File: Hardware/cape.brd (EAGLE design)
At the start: 123 x 126 mm, 38 parts, among them IC2 74VHC541, IC4 74VHC541, IC5 74VHC541, J3 RJ45-8P8C, Q1 N-MOSFET-DUALSO8, Q10 N-MOSFET-DUALSO8, Q11 N-MOSFET-DUALSO8, Q12 N-MOSFET-DUALSO8, Q13 N-MOSFET-DUALSO8, Q14 N-MOSFET-DUALSO8, Q15 N-MOSFET-DUALSO8, Q16 N-MOSFET-DUALSO8, Q2 N-MOSFET-DUALSO8, Q3 N-MOSFET-DUALSO8, Q4 N-MOSFET-DUALSO8, Q5 N-MOSFET-DUALSO8, Q6 N-MOSFET-DUALSO8, Q7 N-MOSFET-DUALSO8, Q8 N-MOSFET-DUALSO8, Q9 N-MOSFET-DUALSO8

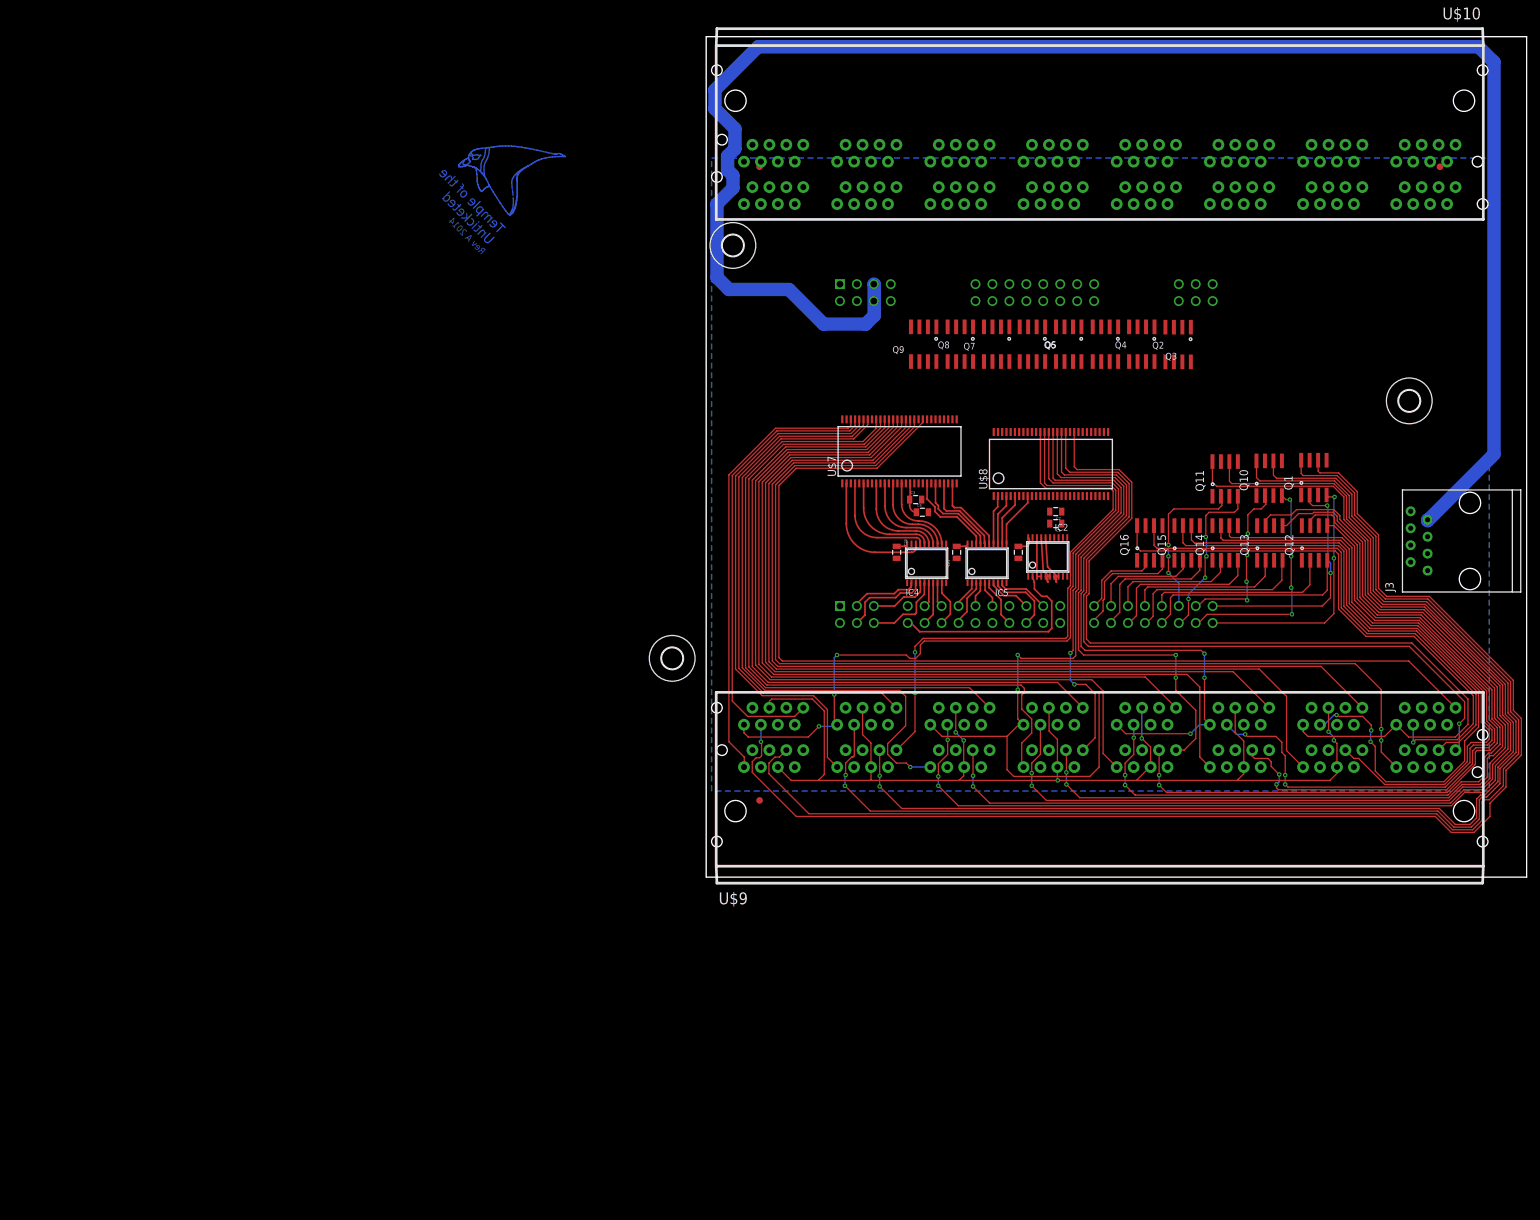
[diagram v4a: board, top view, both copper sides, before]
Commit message: Ripped up, starting over with new buffers
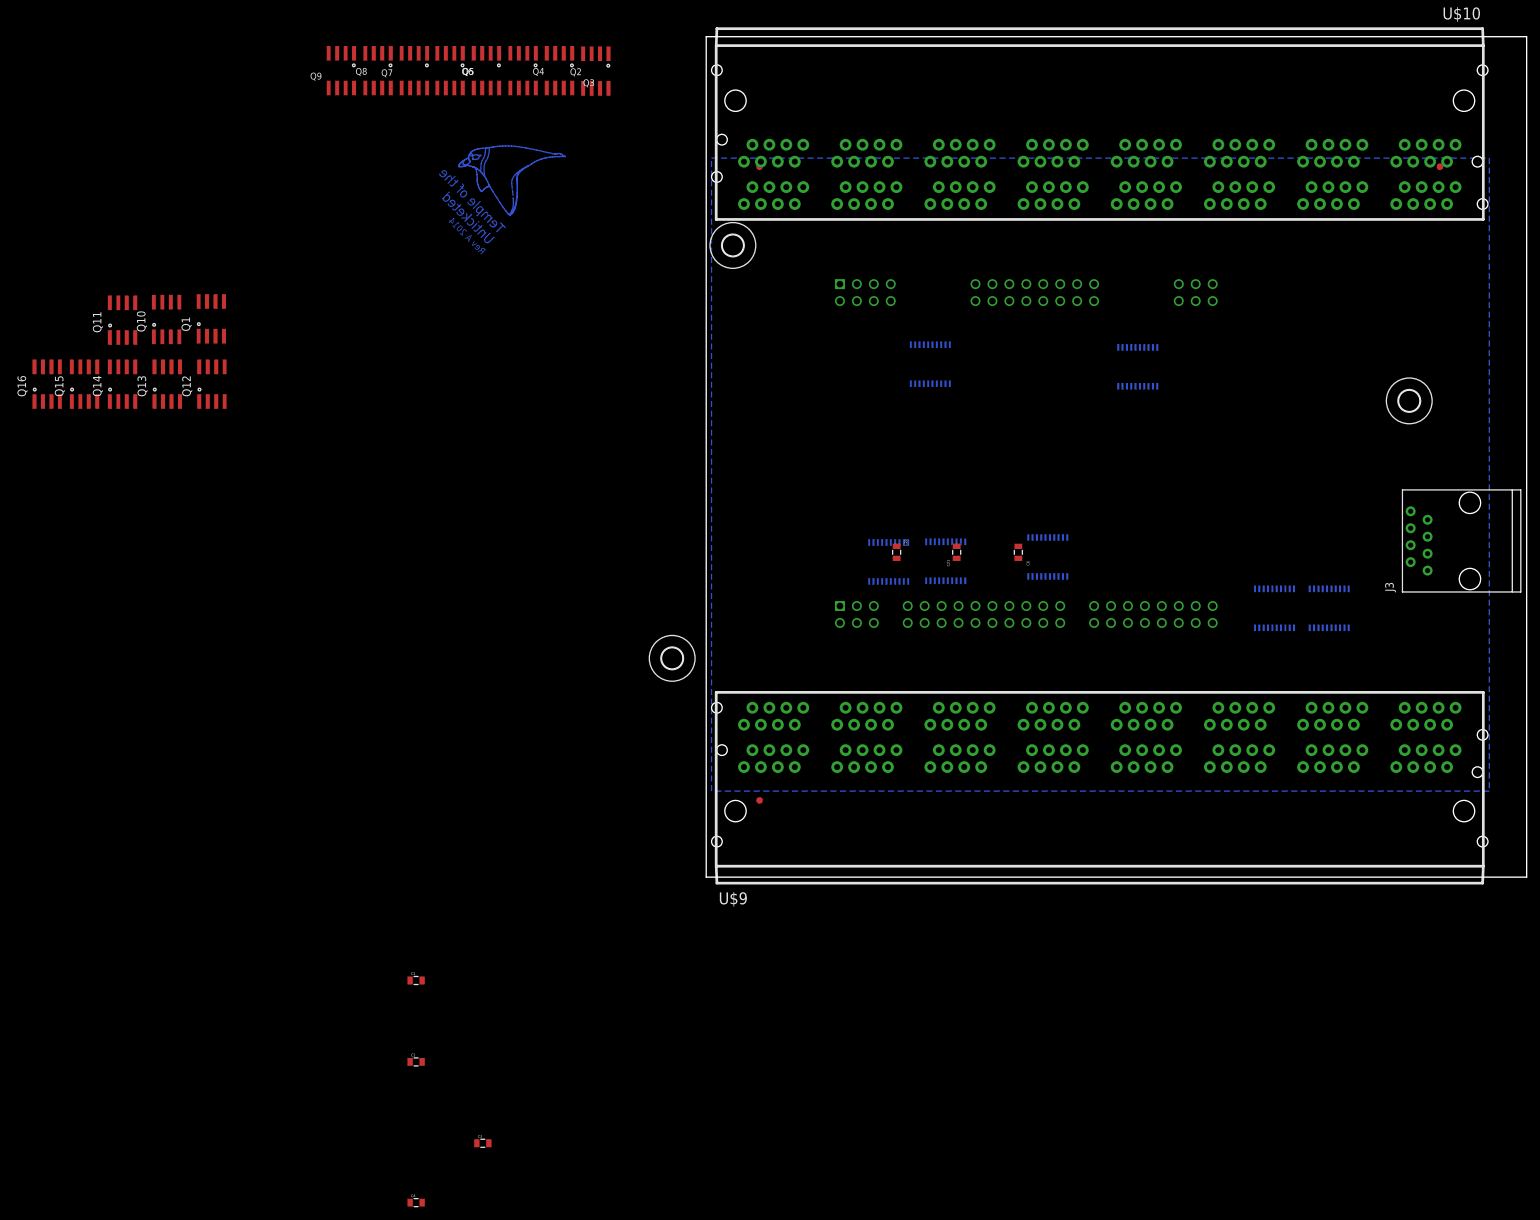
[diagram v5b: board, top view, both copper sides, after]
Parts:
- removed U$7, U$8: SN74CBT16292DLRSSOP56, cape:SSOP56
- added IC1, IC3, IC6, IC7: 74VHC541, cape:TSSOP20
- C1, C4: value 10uF -> 1uF
- moved Q1 167.0 mm to (-74.2, 75.7)
- moved Q10 167.0 mm to (-80.9, 75.6)
- moved Q11 167.0 mm to (-87.5, 75.5)
- moved Q12 167.0 mm to (-74.1, 65.9)
- moved Q13 167.0 mm to (-80.8, 65.9)
- moved Q14 167.0 mm to (-87.5, 65.9)
- moved Q15 167.0 mm to (-93.2, 65.9)
- moved Q16 167.0 mm to (-98.8, 65.9)
- moved C4 128.3 mm to (-43.5, -56.8)
- moved C2 126.5 mm to (-43.5, -35.7), turned to 0 degrees
- moved C1 117.9 mm to (-43.5, -23.5), turned to 0 degrees
- moved C3 116.3 mm to (-33.5, -47.9)
- moved Q2 96.4 mm to (-16.6, 112.8)
- moved Q3 96.4 mm to (-22.0, 112.9)
- moved Q4 96.4 mm to (-27.4, 112.9)
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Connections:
- removed net 17A: IC2.15, U$8.11, U$8.13
- removed net 19A: IC2.14, U$8.15, U$8.18
- removed net 1A: IC4.18, U$7.2
- removed net 21A: IC2.13, U$8.21, U$8.23
- removed net 23A: IC2.12, U$8.25, U$8.27
- removed net 2A: IC4.17, U$7.4
- removed net 3A: IC4.16, U$7.6
- removed net 4A: IC4.15, U$7.9
- removed net 5A: IC4.14, U$7.11
- removed net 6A: IC4.13, U$7.13
- removed net 7A: IC4.12, U$7.15
- removed net 8A: IC4.11, U$7.18
- removed net SCL_1: IC2.18, IC2.3, IC2.4
- removed net SCL_2: IC2.17, IC2.5, IC2.6
- removed net SCL_3: IC2.16, IC2.7, IC2.8
- new net BUF0: IC5.11
- new net BUF1: IC5.12
- new net BUF10: IC4.11
- new net BUF11: IC5.16
- new net BUF12: IC4.13
- new net BUF13: IC4.14
- new net BUF14: IC5.17
- new net BUF15: IC5.18
- new net BUF2: IC4.16
- new net BUF3: IC4.15
- new net BUF4: IC5.13
- new net BUF5: IC5.14
- new net BUF6: IC4.18
- new net BUF7: IC4.17
- new net BUF8: IC5.15
- new net BUF9: IC4.12
- new net SCL_BUF_1: IC1.2, IC2.18, IC3.2
- new net SCL_BUF_2: IC2.17, IC6.2, IC7.2
- net 10A: now also IC1.17, IC3.17, IC6.17, IC7.17; no longer IC5.17, U$7.23
- net 11A: now also IC1.16, IC3.16, IC6.16, IC7.16; no longer IC5.16, U$7.25
- net 12A: now also IC1.15, IC3.15, IC6.15, IC7.15; no longer IC5.15, U$7.27
- net 13A: now also IC1.14, IC3.14, IC6.14, IC7.14; no longer IC5.14, U$8.2
- net 14A: now also IC1.13, IC3.13, IC6.13, IC7.13; no longer IC5.13, U$8.4
- net 15A: now also IC1.12, IC3.12, IC6.12, IC7.12; no longer IC5.12, U$8.6
- net 16A: now also IC1.11, IC3.11, IC6.11, IC7.11; no longer IC5.11, U$8.9
- net 9A: now also IC1.18, IC3.18, IC6.18, IC7.18; no longer IC5.18, U$7.21
- net DATA-0-1: no longer U$8.47
- net DATA-0-2: no longer U$8.46
- net DATA-1-1: no longer U$8.50
- net DATA-1-2: no longer U$8.48
- net DATA-10-1: no longer U$7.39
- net DATA-10-2: no longer U$7.37
- net DATA-11-1: no longer U$7.32
- net DATA-11-2: no longer U$7.31
- net DATA-12-1: no longer U$7.43
- net DATA-12-2: no longer U$7.42
- net DATA-13-1: no longer U$7.45
- net DATA-13-2: no longer U$7.44
- net DATA-14-1: no longer U$7.34
- net DATA-14-2: no longer U$7.33
- net DATA-15-1: no longer U$7.36
- net DATA-15-2: no longer U$7.35
- net DATA-2-1: no longer U$7.50
- net DATA-2-2: no longer U$7.48
- net DATA-3-1: no longer U$7.47
- net DATA-3-2: no longer U$7.46
- net DATA-4-1: no longer U$8.52
- net DATA-4-2: no longer U$8.51
- net DATA-5-1: no longer U$8.54
- net DATA-5-2: no longer U$8.53
- net DATA-6-1: no longer U$7.54
- net DATA-6-2: no longer U$7.53
- net DATA-7-1: no longer U$7.52
- net DATA-7-2: no longer U$7.51
- net DATA-8-1: no longer U$7.30
- net DATA-8-2: no longer U$7.29
- net DATA-9-1: no longer U$7.41
- net DATA-9-2: no longer U$7.40
- net GND: now also IC1.10, IC3.10, IC6.10, IC7.10; no longer U$7.19, U$7.38, U$7.49, U$7.8, U$8.19, U$8.38, U$8.49, U$8.8
- net MUX_S: no longer U$7.1, U$8.1
- net SCL-A-1: no longer U$8.45
- net SCL-A-2: no longer U$8.44
- net SCL-B-1: no longer U$8.43
- net SCL-B-2: no longer U$8.42
- net SCL-C-1: no longer U$8.41
- net SCL-C-2: no longer U$8.40
- net SCL-D-1: no longer U$8.39
- net SCL-D-2: no longer U$8.37
- net SCL-E-1: no longer U$8.36
- net SCL-E-2: no longer U$8.35
- net SCL-F-1: no longer U$8.34
- net SCL-F-2: no longer U$8.33
- net SCL-G-1: no longer U$8.32
- net SCL-G-2: no longer U$8.31
- net SCL-H-1: no longer U$8.30
- net SCL-H-2: no longer U$8.29
- net SCL_RAW: now also IC2.3
- net VCC3V3: now also C1.1, C2.1, C3.1, C4.1, IC1.20, IC3.20, IC6.20, IC7.20
- net VCC5V: no longer C1.1, C2.1, C3.1, C4.1, U$7.17, U$8.17
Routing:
- net VCC5V: track 261.1 -> 0.00 mm
- net BL-6-2: track 196.7 -> 0.00 mm, vias 1 -> 0
- net BL-6-1: track 193.0 -> 0.00 mm
- net BL-7-2: track 188.4 -> 0.00 mm, vias 2 -> 0
- net BL-7-1: track 180.1 -> 0.00 mm, vias 2 -> 0
- net RST: track 175.3 -> 0.00 mm, vias 6 -> 0
- net BL-2-2: track 175.1 -> 0.00 mm, vias 3 -> 0
- net BL-2-1: track 166.9 -> 0.00 mm, vias 2 -> 0
- net DATA-10-1: track 156.9 -> 0.00 mm, vias 2 -> 0
- net DATA-10-2: track 156.3 -> 0.00 mm
- net BL-3-2: track 148.2 -> 0.00 mm, vias 2 -> 0
- net DATA-9-1: track 143.3 -> 0.00 mm
- net DATA-9-2: track 143.3 -> 0.00 mm
- net SCL-D-2: track 134.2 -> 0.00 mm
- net BL-3-1: track 134.1 -> 0.00 mm, vias 2 -> 0
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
